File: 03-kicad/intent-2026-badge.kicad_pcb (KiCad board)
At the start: 2 copper layers, 56 x 125.5 mm, 94 parts, among them J1 TYPE-C-31-M-12, J2 HACK HEADER, J3 BATT 3xAAA, J5 SAO1 IR, J6 SAO2 IMU, J7 SAO3 SPK, P1 IR MODULE, P2 IMU MODULE, P3 SPK MODULE, Q1 HL3401, Q2 S8050, SW1 BOOTSEL, SW2 A, SW3 B, SW4 C, SW6 RESET, U1 RP2040, U2 W25Q16JVSNIQ, U3 AP2112K-3.3TRG1, U4 USBLC6-2SC6, U5 IRM-H638T/TR2, U6 SN74LV1T34DBVR, U7 LSM6DS3TR-C, Y1 12MHz ABM8-272-T3

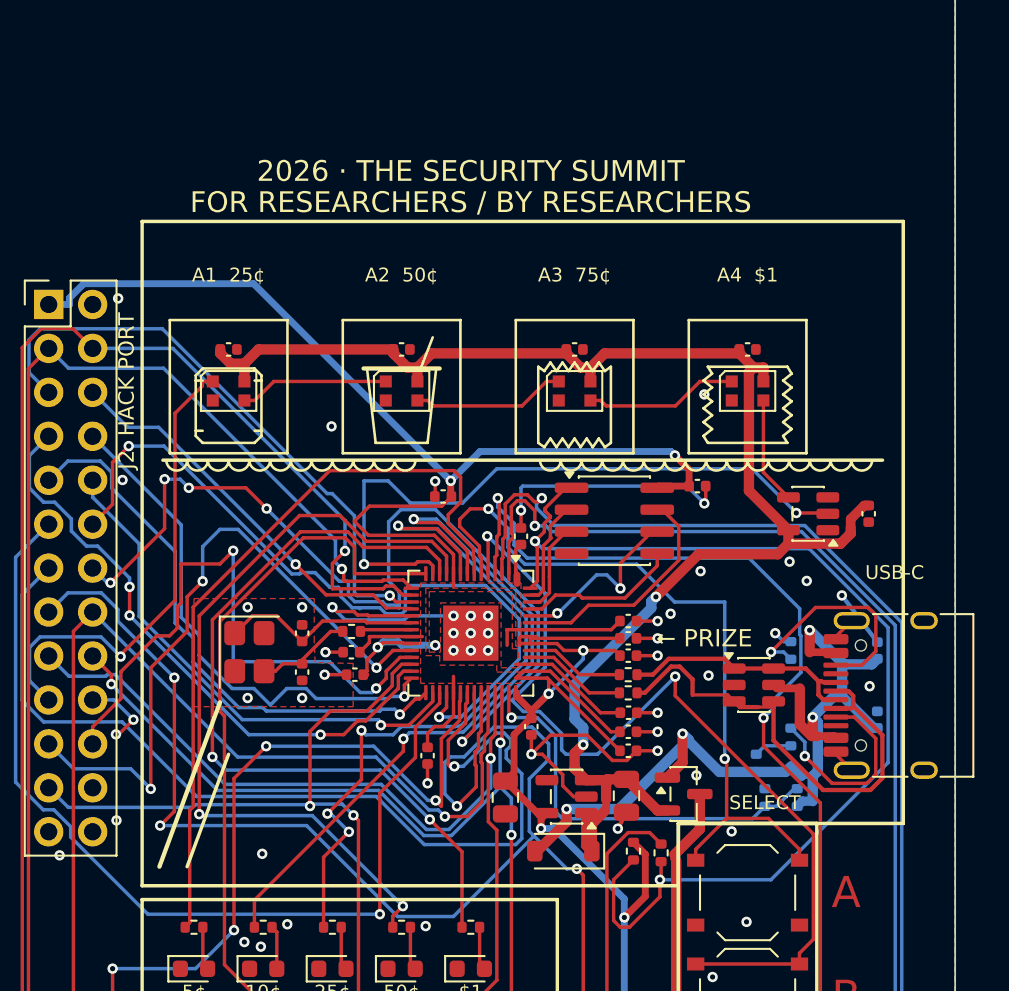
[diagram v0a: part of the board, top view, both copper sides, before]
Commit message: Add J8, 4-pin I2C socket for a 0.96" OLED module
- J8: 1x4 2.54 mm SMD female socket (C42379197), 1 GND, 2 3V3, 3 SCL,
  4 SDA on the SAO I2C bus; placed by Benny under the logo.
- Routed locally to the existing +3V3 / SAO_SCL / SAO_SDA copper.
  DRC 0 errors, 0 unconnected. 04-fab regenerated; BOM deltas EN/HE,
  BUILD-NOTES item 22.

Co-Authored-By: Claude Opus 5.5 (1M context) <noreply@anthropic.com>
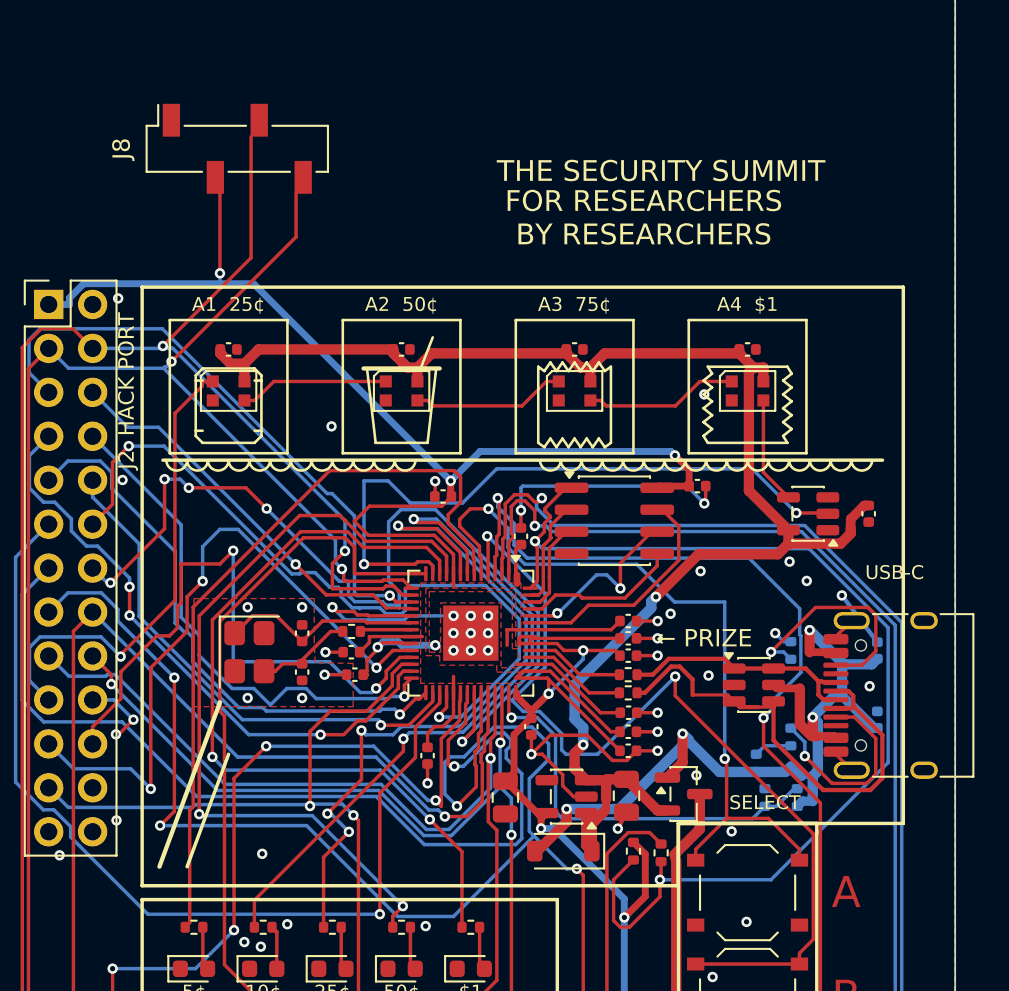
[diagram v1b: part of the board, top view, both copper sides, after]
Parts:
- added J8: OLED 0.96 I2C, Connector_PinSocket_2.54mm:PinSocket_1x04_P2.54mm_Vertical_SMD_Pin1Right, F.Cu at (114.5, 72.0)
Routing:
- net SAO_SCL: track 129.7 -> 144.4 mm, vias 4 -> 5
- net SAO_SDA: track 116.8 -> 130.0 mm, vias 4 -> 5
- net +3V3: track 212.5 -> 217.6 mm, vias 14 -> 15
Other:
- board text added: "FOR RESEARCHERS BY RESEARCHERS"
- board text added: "THE SECURITY SUMMIT"
- board text removed: "2026 · THE SECURITY SUMMIT"
- board text removed: "FOR RESEARCHERS / BY RESEARCHERS"

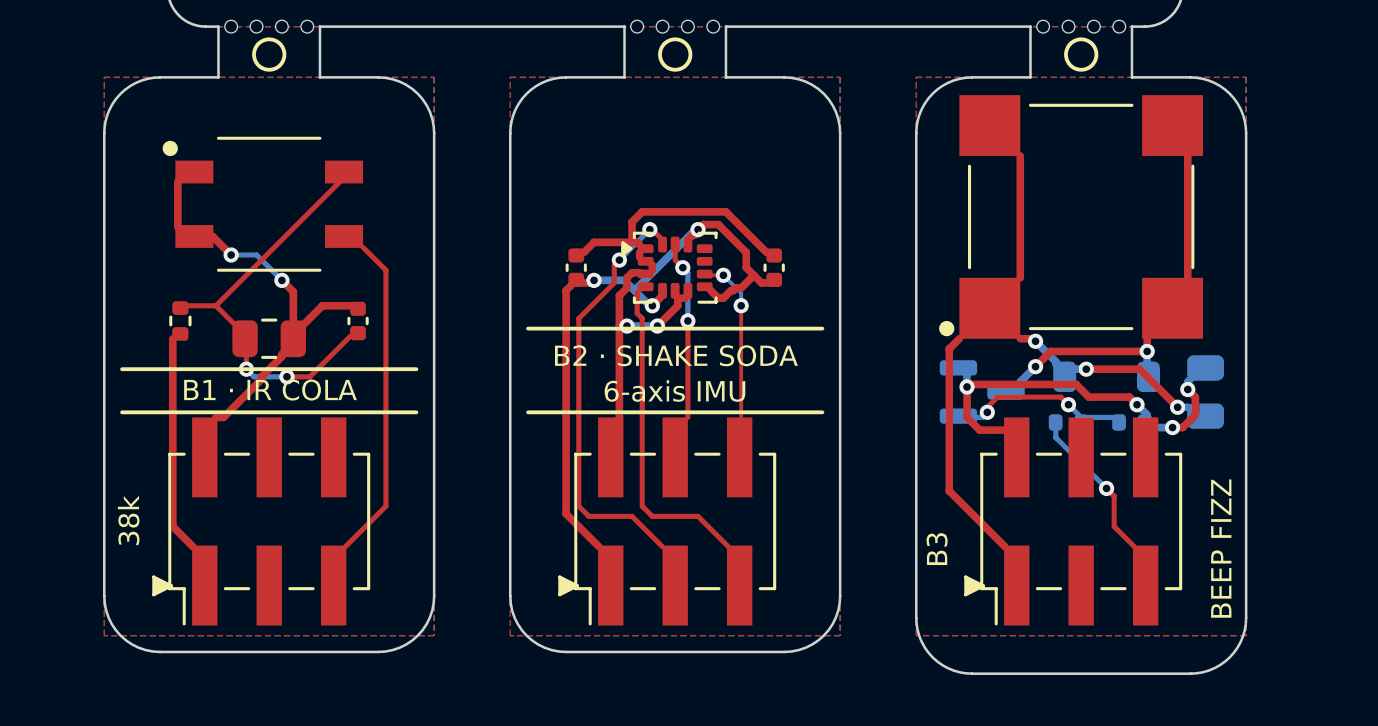
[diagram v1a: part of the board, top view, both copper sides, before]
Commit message: Module SAO headers to the can backs; order spec for two-sided SMT assembly
P1-P3 move to B.Cu (rot 270, same pad pattern as J5-J7) so the modules plug in
face-up. Speaker driver row back on the front, module silk adjusted, module nets
re-routed. DRC 0 errors / 0 unconnected; fab outputs regenerated.

Co-Authored-By: Claude Opus 5.5 (1M context) <noreply@anthropic.com>
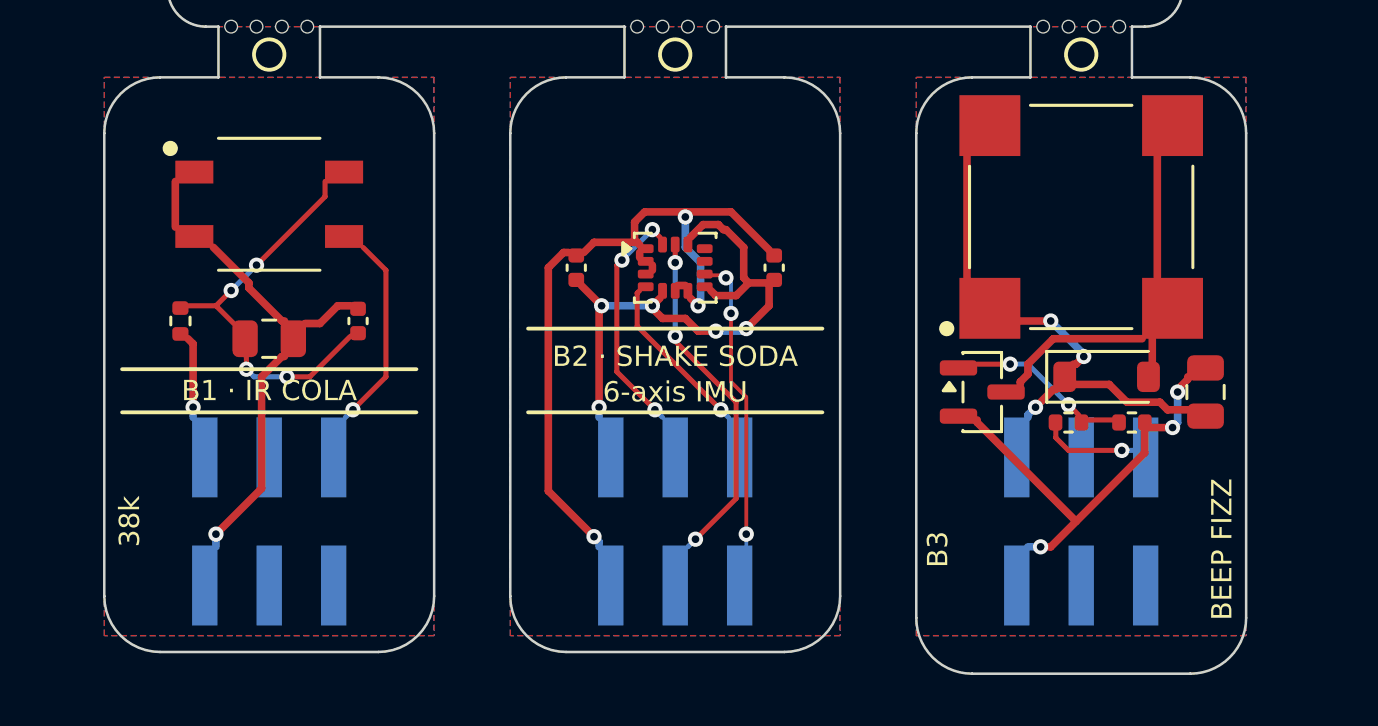
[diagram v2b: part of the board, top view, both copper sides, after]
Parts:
- C25, D7, Q2, R20, R21: moved to F.Cu
- P1, P2, P3: moved to B.Cu
- turned P1 to -90 degrees
- turned P2 to -90 degrees
- turned P3 to -90 degrees
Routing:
- net IMM_GND: track 19.2 -> 27.3 mm, vias 2 -> 3
- net IMM_SDA: track 16.5 -> 9.15 mm, vias 2 -> 3
- net IMM_SCL: track 6.71 -> 13.4 mm, vias 2 -> 3
- net IMM_INT1: track 12.7 -> 6.53 mm, vias 0 -> 1
- net SPM_3V3: track 21.0 -> 14.9 mm
- net IRM_3V3: track 8.53 -> 3.18 mm, vias 0 -> 1
- net IMM_INT2: track 6.39 -> 11.6 mm, vias 2 -> 3
- net IRM_OUT: track 12.8 -> 7.74 mm, vias 0 -> 1
- net IMM_3V3: track 24.8 -> 21.0 mm, vias 3 -> 5
- net IRM_GND: track 14.3 -> 16.7 mm, vias 2 -> 1
- net SPM_SIG: track 5.88 -> 3.61 mm
- net SPM_GND: track 14.6 -> 15.8 mm, vias 4 -> 3
- net IRM_VCC: track 14.8 -> 14.2 mm, vias 2 -> 4
- net SPM_COL: track 11.3 -> 11.5 mm, vias 2 -> 0

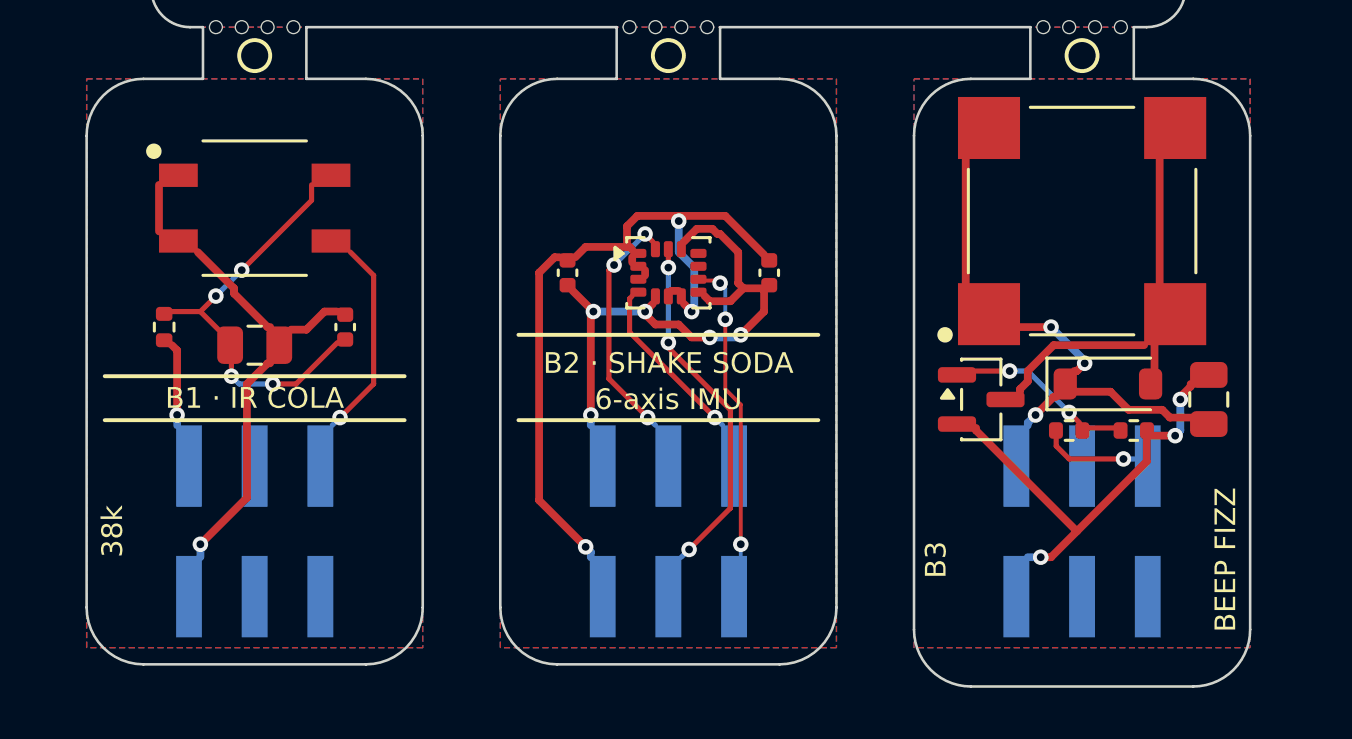
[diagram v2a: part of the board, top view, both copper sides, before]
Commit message: Module SAO headers turned 180 deg so the plugged modules hang down
P1-P3 stay on the can backs at rot 90 (pin 1 bottom-right seen from the front); a
module plugs in face-up below its socket instead of covering D1-D5. Back pin-1
marks moved, module nets re-routed. DRC 0 errors / 0 unconnected; fab outputs
regenerated.

Co-Authored-By: Claude Opus 5.5 (1M context) <noreply@anthropic.com>
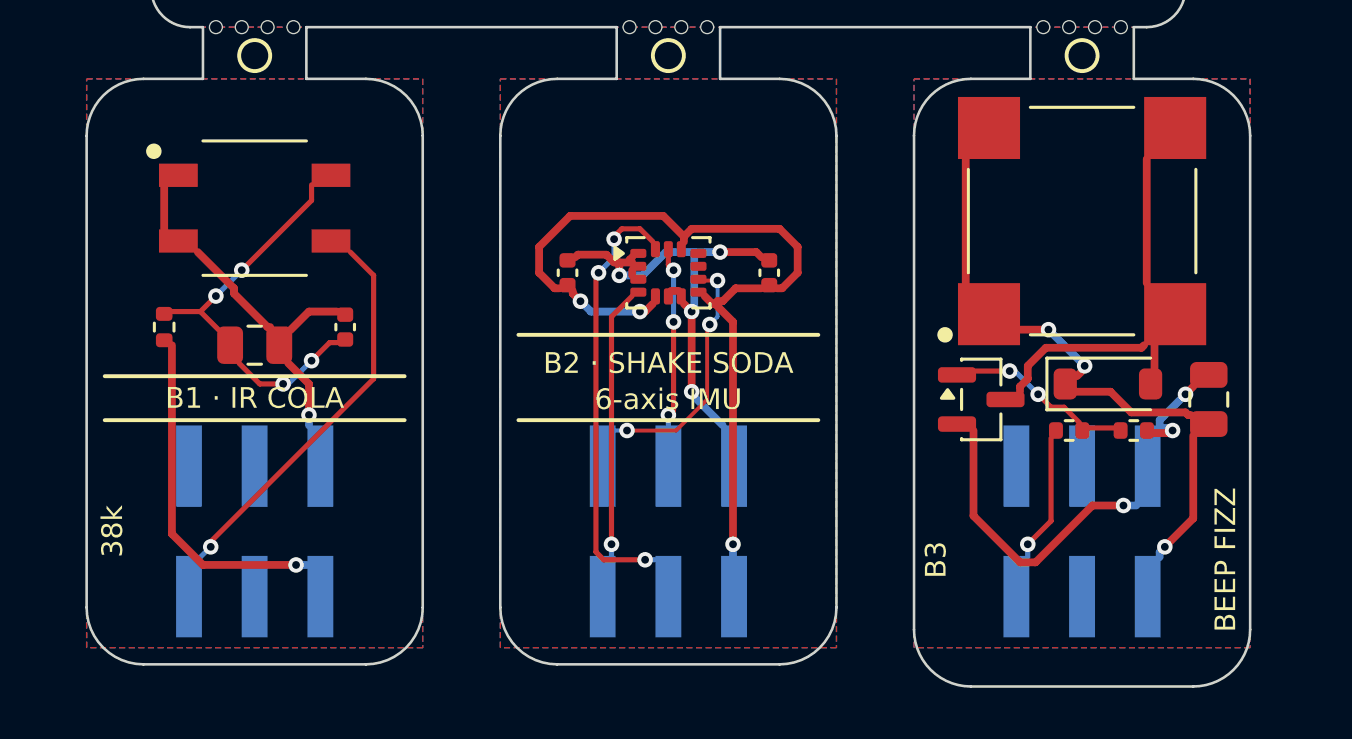
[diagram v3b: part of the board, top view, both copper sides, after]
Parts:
- turned P1 to 90 degrees
- turned P2 to 90 degrees
- turned P3 to 90 degrees
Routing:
- net IMM_3V3: track 21.0 -> 31.8 mm, vias 5 -> 3
- net IMM_GND: track 27.3 -> 17.2 mm, vias 3 -> 4
- net IRM_3V3: track 3.18 -> 13.1 mm
- net IMM_SDA: track 9.15 -> 16.7 mm
- net IRM_OUT: track 7.74 -> 14.9 mm
- net IMM_SCL: track 13.4 -> 6.67 mm
- net IRM_GND: track 16.7 -> 10.7 mm
- net IMM_INT1: track 6.53 -> 10.4 mm
- net SPM_3V3: track 14.9 -> 18.4 mm
- net IMM_INT2: track 11.6 -> 9.36 mm
- net SPM_SIG: track 3.61 -> 4.97 mm
- net SPM_GND: track 15.8 -> 14.7 mm
- net IRM_VCC: track 14.2 -> 13.6 mm

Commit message: Module can art turned 180 deg to read upright when plugged in; IMU front pour restored
Front can texts rotated (silk.py + board). 11 IMM_GND stitching vias bring back
the IMU can's front ground pour, which the last re-route had left as a removed
island. DRC 0 errors / 0 unconnected; fab outputs regenerated.

Co-Authored-By: Claude Opus 5.5 (1M context) <noreply@anthropic.com>
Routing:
- net IMM_GND: vias 4 -> 15
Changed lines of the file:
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@@
-		)
-	)
-	(gr_text "B1 · IR COLA"
-		(at 112 164.35 0)
-		(layer "F.SilkS")
-		(effects
-			(font
-				(size 0.8 0.8)
-				(thickness 0.15)
-			)
 		)
 	)
@@
 		)
 	)
-	(gr_text "B2 · SHAKE SODA"
-		(at 128 163 0)
-		(layer "F.SilkS")
-		(effects
-			(font
-				(size 0.8 0.8)
-				(thickness 0.15)
-			)
-		)
-	)
-	(gr_text "6-axis IMU"
-		(at 128 164.4 0)
-		(layer "F.SilkS")
-		(effects
-			(font
-				(size 0.8 0.8)
-				(thickness 0.15)
-			)
-		)
-	)
 	(gr_text "B3 SPK"
 		(at 131.96 129.32 0)
@@
 		)
 	)
+	(gr_text "B1 · IR COLA"
+		(at 112 164.35 180)
+		(layer "F.SilkS")
+		(effects
+			(font
+				(size 0.8 0.8)
+				(thickness 0.15)
+			)
+		)
+	)
+	(gr_text "6-axis IMU"
+		(at 128 162.7 180)
+		(layer "F.SilkS")
+		(effects
+			(font
+				(size 0.8 0.8)
+				(thickness 0.15)
+			)
+		)
+	)
+	(gr_text "B2 · SHAKE SODA"
+		(at 128 164.1 180)
+		(layer "F.SilkS")
+		(effects
+			(font
+				(size 0.8 0.8)
+				(thickness 0.15)
+			)
+		)
+	)
 	(gr_text "38k"
-		(at 106.5 169.5 90)
+		(at 117.5 169.5 270)
+		(layer "F.SilkS")
+		(effects
+			(font
+				(size 0.8 0.8)
+				(thickness 0.15)
+			)
+		)
+	)
+	(gr_text "BEEP FIZZ"
+		(at 138.45 170.6 270)
 		(layer "F.SilkS")
 		(effects
@@
 	)
 	(gr_text "B3"
-		(at 138.35 170.6 90)
-		(layer "F.SilkS")
-		(effects
-			(font
-				(size 0.8 0.8)
-				(thickness 0.15)
-			)
-		)
-	)
-	(gr_text "BEEP FIZZ"
-		(at 149.55 170.6 90)
+		(at 149.65 170.6 270)
 		(layer "F.SilkS")
 		(effects
@@
 	)
 	(via
+		(at 124.5 158)
+		(size 0.6)
+		(drill 0.3)
+		(layers "F.Cu" "B.Cu")
+		(net "IMM_GND")
+	)
+	(via
 		(at 128.9 164.1)
 		(size 0.6)
@@
 	)
 	(via
+		(at 132.3 155.5)
+		(size 0.6)
+		(drill 0.3)
+		(layers "F.Cu" "B.Cu")
+		(net "IMM_GND")
+	)
+	(via
+		(at 132.699999 171)
+		(size 0.6)
+		(drill 0.3)
+		(layers "F.Cu" "B.Cu")
+		(net "IMM_GND")
+	)
+	(via
+		(at 129.27 169.5)
+		(size 0.6)
+		(drill 0.3)
+		(layers "F.Cu" "B.Cu")
+		(net "IMM_GND")
+	)
+	(via
+		(at 123.3 168)
+		(size 0.6)
+		(drill 0.3)
+		(layers "F.Cu" "B.Cu")
+		(net "IMM_GND")
+	)
+	(via
+		(at 123.7 155.5)
+		(size 0.6)
+		(drill 0.3)
+		(layers "F.Cu" "B.Cu")
+		(net "IMM_GND")
+	)
+	(via
+		(at 123.3 164)
+		(size 0.6)
+		(drill 0.3)
+		(layers "F.Cu" "B.Cu")
+		(net "IMM_GND")
+	)
+	(via
+		(at 123.3 171)
+		(size 0.6)
+		(drill 0.3)
+		(layers "F.Cu" "B.Cu")
+		(net "IMM_GND")
+	)
+	(via
 		(at 128.9 161)
 		(size 0.6)
@@
 	)
 	(via
+		(at 126.73 169.5)
+		(size 0.6)
+		(drill 0.3)
+		(layers "F.Cu" "B.Cu")
+		(net "IMM_GND")
+	)
+	(via
+		(at 132.699999 164)
+		(size 0.6)
+		(drill 0.3)
+		(layers "F.Cu" "B.Cu")
+		(net "IMM_GND")
+	)
+	(via
 		(at 126.1 159.6)
 		(size 0.6)
 		(drill 0.3)
+		(layers "F.Cu" "B.Cu")
+		(net "IMM_GND")
+	)
+	(via
+		(at 132.699999 168)
+		(size 0.6)
+		(drill 0.3)
